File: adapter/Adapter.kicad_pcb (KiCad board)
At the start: 4 copper layers, 50 parts, among them J1 USB_B_Micro, J2 2040210-1, J3 USB_C_Receptacle, J4 Conn_01x05_Male, Q1 IRLML2244TRPBF, SW1 SW_Push, SW2 SW_Push, U1 SN75DP119, U2 AZ1117-3.3, U3 STM32F072C8Tx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

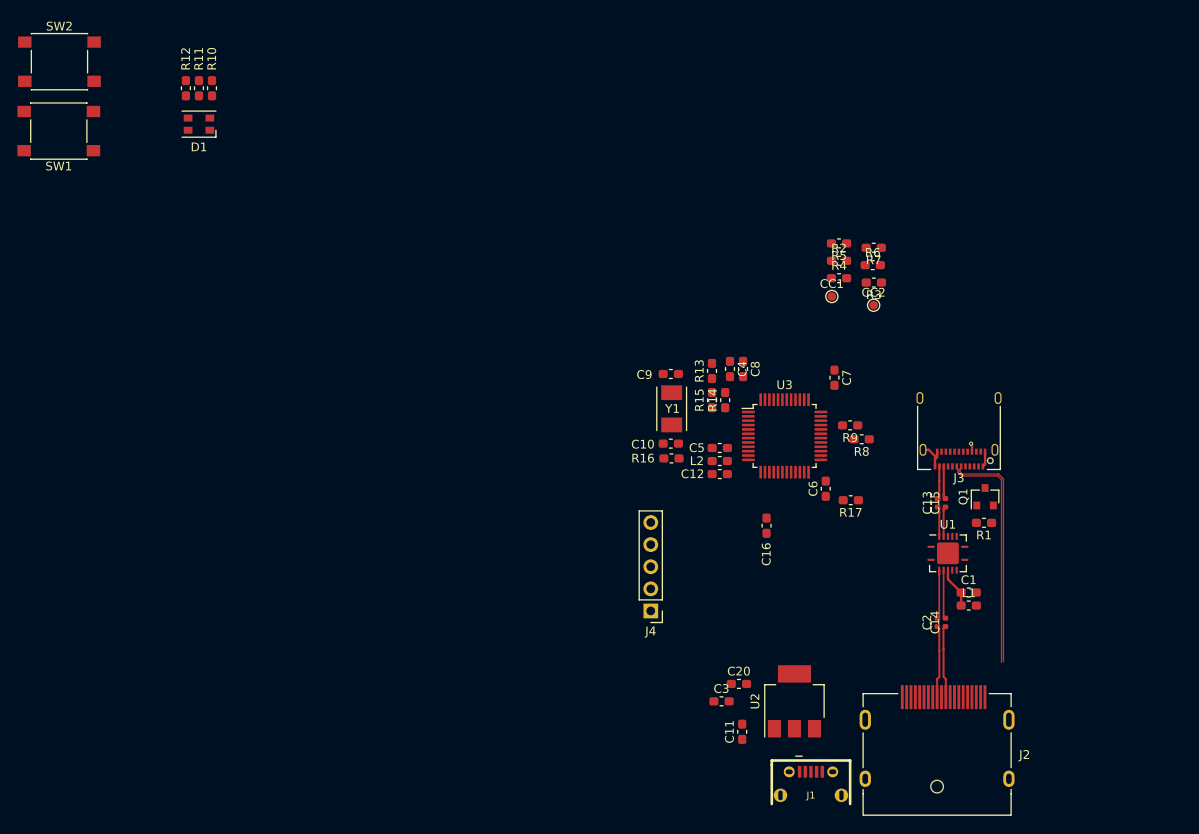
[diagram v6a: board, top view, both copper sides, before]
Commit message: renamed custom footprints
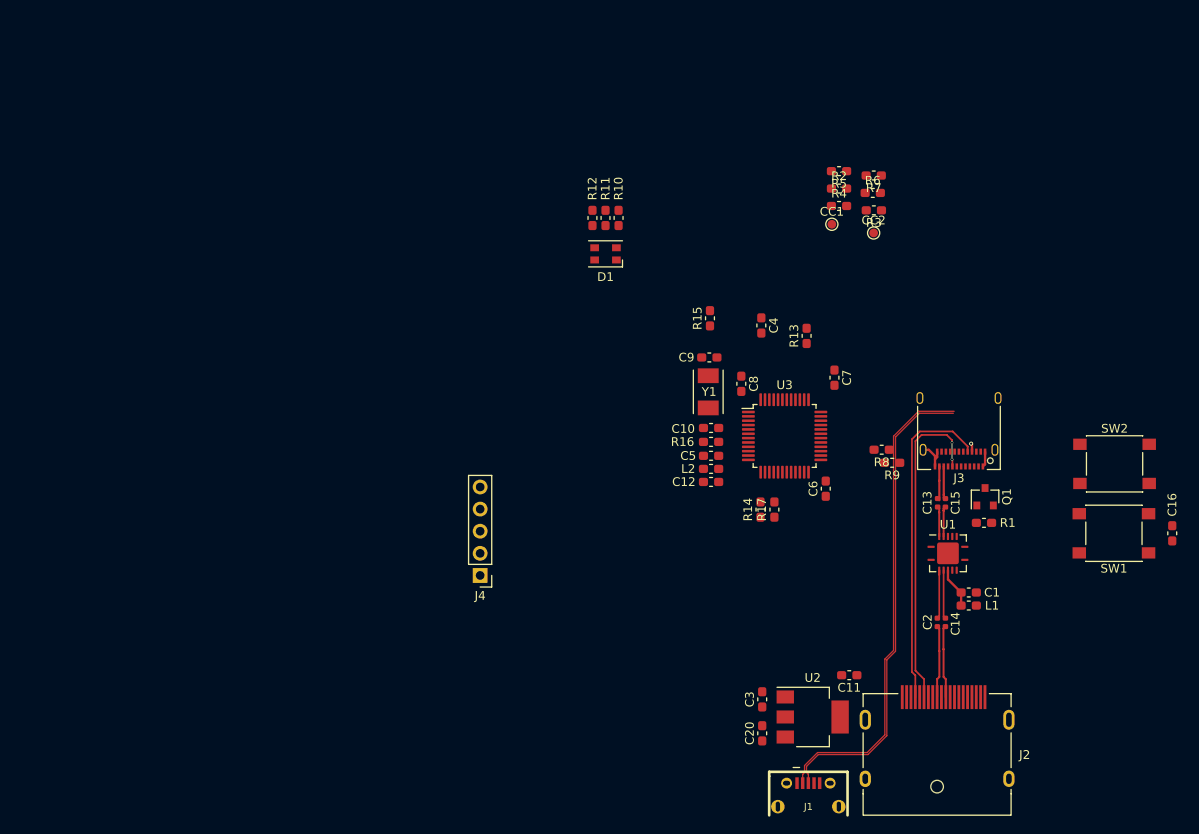
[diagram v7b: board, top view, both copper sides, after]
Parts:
- J2: footprint DP1RD20JQ1R400:DP1RD20JQ1R400 -> Displayport:DP1RD20JQ1R400
- U1: footprint SN75DP118:QFN-20-1EP_4x4mm_P0.5mm_EP2.5x2.5mm -> SN75DP119:QFN-20-1EP_4x4mm_P0.5mm_EP2.5x2.5mm
- moved SW1 129.7 mm to (74.0, 51.5)
- moved SW2 129.7 mm to (74.1, 43.5)
- moved D1 49.0 mm to (15.6, 19.4)
- moved R10 49.0 mm to (17.1, 15.3)
- moved R11 49.0 mm to (15.6, 15.3)
- moved R12 49.0 mm to (14.1, 15.3)
- moved C16 46.6 mm to (80.7, 51.5), turned to 270 degrees
- moved J4 20.0 mm to (1.20, 56.3)
- moved C11 13.9 mm to (43.6, 67.8), turned to 180 degrees
- moved R14 13.2 mm to (33.4, 48.8)
- moved R13 11.6 mm to (38.7, 28.8)
- moved R15 9.41 mm to (27.6, 26.8)
- moved R17 8.84 mm to (35.0, 48.8), turned to 90 degrees
- moved CC1 8.30 mm to (41.6, 16.0)
- moved CC2 8.30 mm to (46.4, 17.0)
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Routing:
- net /AUX-: track 0.00 -> 37.9 mm
- net /AUX+: track 0.00 -> 37.6 mm, vias 0 -> 2
- net /D-: track 27.1 -> 55.7 mm
- net /D+: track 27.0 -> 55.2 mm

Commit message: more 3d packages...
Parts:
- added C17: 100n, Capacitor_SMD:C_0603_1608Metric_Pad1.05x0.95mm_HandSolder, F.Cu at (56.3, 48.8)
- added J5: Conn_01x03_Male, Connector_Molex:Molex_PicoBlade_53047-0310_1x03_P1.25mm_Vertical, F.Cu at (36.2, 35.3)
- J4: footprint Connector_PinHeader_2.54mm:PinHeader_1x05_P2.54mm_Vertical -> Connector_Molex:Molex_PicoBlade_53047-0510_1x05_P1.25mm_Vertical
- SW1, SW2: footprint Button_Switch_SMD:SW_SPST_PTS645 -> EVQPLMA15:EVQPLMA15
- moved R12 59.6 mm to (68.3, 40.0), turned to 270 degrees
- moved R11 56.9 mm to (66.8, 40.0), turned to 270 degrees
- moved R10 54.2 mm to (65.3, 40.0), turned to 270 degrees
- moved D1 53.8 mm to (66.8, 35.9), turned to 0 degrees
- moved R13 49.9 mm to (67.0, 69.9), turned to 180 degrees
- moved J4 47.1 mm to (43.5, 35.5), turned to 0 degrees
- moved R7 37.8 mm to (37.1, 47.0), turned to 0 degrees
- moved R5 37.2 mm to (41.0, 47.0)
- moved R6 34.4 mm to (37.1, 45.5), turned to 180 degrees
- moved R2 33.6 mm to (41.0, 45.5), turned to 180 degrees
- moved R3 31.0 mm to (37.1, 44.0), turned to 0 degrees
- moved R4 30.1 mm to (41.0, 44.0)
- moved CC2 26.5 mm to (37.9, 42.1), turned to 180 degrees
- moved CC1 26.2 mm to (40.4, 42.1), turned to 180 degrees
- moved C16 24.2 mm to (67.0, 71.5), turned to 0 degrees
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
